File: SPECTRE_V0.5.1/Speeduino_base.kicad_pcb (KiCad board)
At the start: 2 copper layers, 100 x 93 mm, 205 parts, among them J1 Conn_01x06_Male, J2 Conn_02x04_Odd_Even, Q1 AO3400, Q12 BSP78, Q13 BSP78, Q14 BSP78, Q15 BSP78, Q18 BSP78, Q19 BSP78, Q2 AO3400, Q20 BSP78, Q23 BSP78, Q24 BSP78, Q25 BSP78, Q26 BSP78, Q27 AO3400, Q28 AO3400, Q3 AO3400, Q4 AO3400, Q5 AO3400, Q6 AO3400, Q7 AO3400, U1 MAX9926UAEE+, U2 LM78M05_TO220, U3 TL431DBZ, U4 molex_48pin, U5 TJA1050, U6 MAX3232

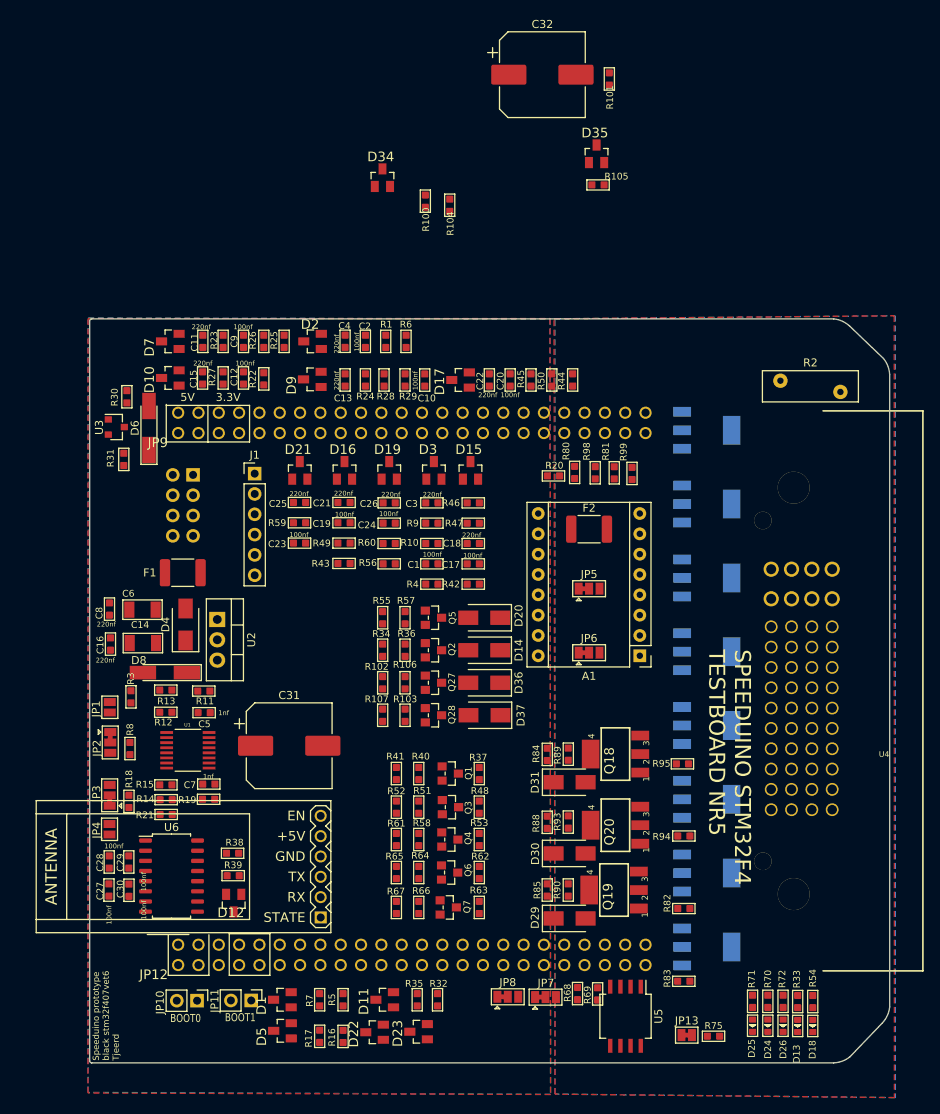
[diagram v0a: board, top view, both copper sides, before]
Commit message: re-add bluetooth module
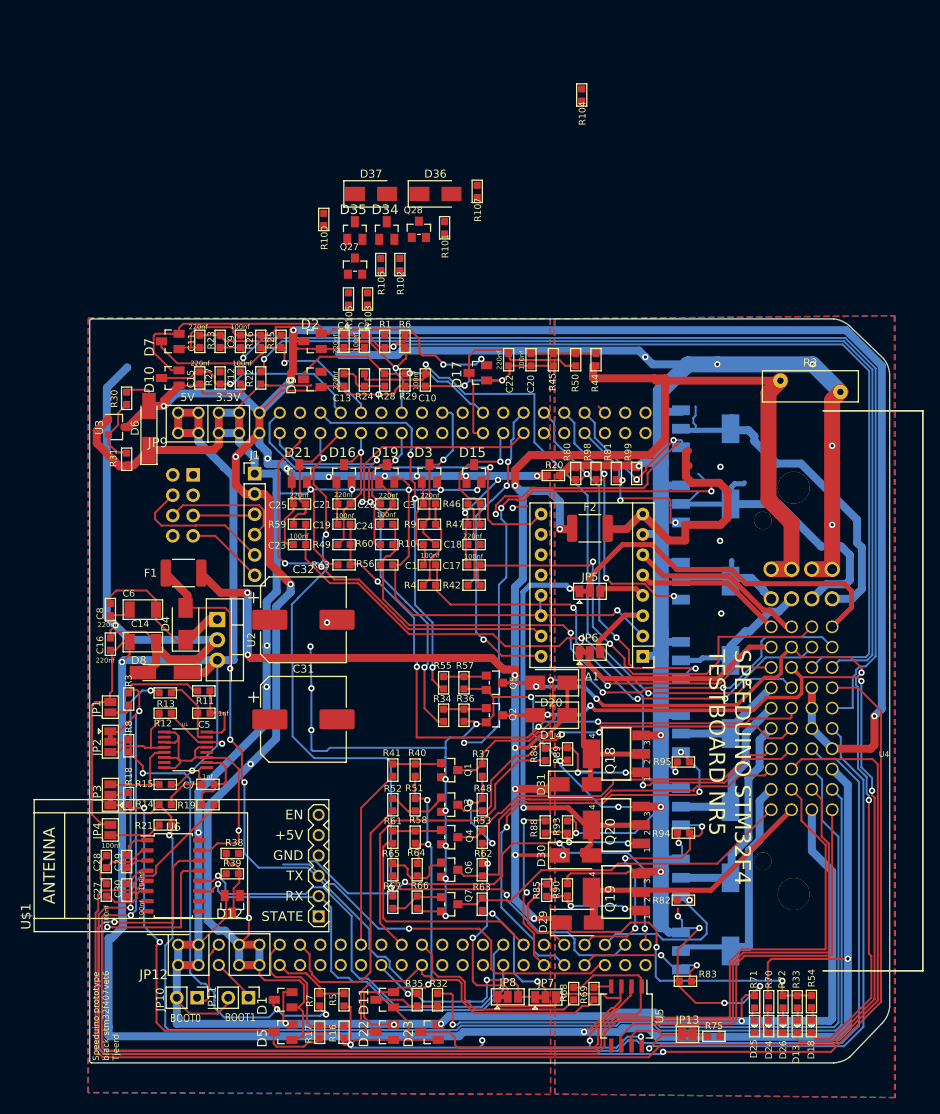
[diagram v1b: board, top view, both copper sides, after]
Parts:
- moved C32 74.4 mm to (140.7, 54.6)
- moved D37 66.7 mm to (149.2, 1.38), turned to 0 degrees
- moved R107 66.5 mm to (162.4, 1.06), turned to 0 degrees
- moved D36 61.4 mm to (157.2, 1.38), turned to 0 degrees
- moved Q28 60.8 mm to (155.2, 5.81), turned to 0 degrees
- moved Q27 53.0 mm to (147.2, 10.4), turned to 0 degrees
- moved R106 52.4 mm to (150.4, 10.2)
- moved R102 52.3 mm to (152.8, 10.2), turned to 0 degrees
- moved R103 52.2 mm to (148.7, 14.5), turned to 0 degrees
- moved R105 34.3 mm to (146.3, 14.5), turned to 0 degrees
- moved D35 31.7 mm to (147.1, 5.95)
- moved R101 27.8 mm to (158.4, 5.61)
- moved R104 21.5 mm to (175.5, -11.0)
- moved R100 12.9 mm to (143.3, 4.57)
- moved D14 11.7 mm to (171.7, 66.5)
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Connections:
- C1 pad 2: AIN_1 -> AIN_2
- C2 pad 2: AIN_0 -> AIN_1
- C24 pad 2: AIN_2 -> AIN_3
- C32 pad 1: Net-(C32-Pad1) -> 5V
- R1 pad 1: AIN_0 -> AIN_1
- R4 pad 1: AIN_1 -> AIN_2
- R56 pad 1: AIN_2 -> AIN_3
- R6 pad 1: AIN_0 -> AIN_1
- R60 pad 1: AIN_2 -> AIN_3
- U4 pad 14: AIN_1 -> AIN_2
- U4 pad 18: AIN_0 -> AIN_1
- U4 pad 20: AIN_2 -> AIN_3
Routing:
- net GND: track 0.00 -> 597.8 mm, vias 0 -> 25
- net 3.3V: track 0.00 -> 467.7 mm, vias 0 -> 18
- net PWR_GND: track 0.00 -> 456.4 mm, vias 0 -> 30
- net 5V: track 0.00 -> 331.9 mm, vias 0 -> 5
- net VBAT: track 0.00 -> 267.2 mm, vias 0 -> 12
- net VR1+: track 0.00 -> 186.2 mm, vias 0 -> 2
- net VR2-: track 0.00 -> 181.9 mm
- net RS232_TX: track 0.00 -> 179.6 mm, vias 0 -> 2
- net VR1-: track 0.00 -> 174.3 mm, vias 0 -> 2
- net RS232_RX: track 0.00 -> 167.9 mm, vias 0 -> 1
- net VR2+: track 0.00 -> 151.8 mm, vias 0 -> 1
- net MAP: track 0.00 -> 132.1 mm, vias 0 -> 1
- net IAT: track 0.00 -> 121.5 mm, vias 0 -> 1
- net AIN_1: track 0.00 -> 111.4 mm, vias 0 -> 1
- net FUEL_PUMP: track 0.00 -> 105.4 mm, vias 0 -> 4
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
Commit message: Clean-up PCB V0.5.1
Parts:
- removed D34, D35: BAT54S, Speeduino_base:SOT23
- removed R100, R101, R104, R105: 1k, Speeduino_base:R0603
- added D27: YEL, Speeduino_base:LED-0603, F.Cu at (165.9, 19.1)
- added JP14: SolderJumper_3_Bridged12, Jumper:SolderJumper-3_P1.3mm_Bridged12_Pad1.0x1.5mm, F.Cu at (194.3, 53.3)
- added JP15: SolderJumper_3_Bridged12, Jumper:SolderJumper-3_P1.3mm_Bridged12_Pad1.0x1.5mm, F.Cu at (190.5, 53.3)
- added Q8: AO3400, Speeduino_base:SOT-23, F.Cu at (158.5, 20.1)
- added R73: 100R, Speeduino_base:R0603, F.Cu at (162.1, 19.1)
- C31, C32: value 1000uF -> 470uF 6.3V; footprint Capacitor_SMD:CP_Elec_10x12.5 -> Capacitor_SMD:CP_Elec_6.3x7.7
- R25: value 4K7 -> 4k7
- R33, R54: value 1k -> 470R
- U2: footprint Package_TO_SOT_THT:TO-220-3_Vertical -> Package_TO_SOT_THT:TO-220-3_Horizontal_TabUp; moved to B.Cu
- moved Q27 55.0 mm to (194.1, 39.1), turned to 270 degrees
- moved D37 49.9 mm to (192.1, 26.9)
- moved R106 49.6 mm to (190.8, 39.1)
- moved D36 48.8 mm to (192.1, 35.6)
- moved Q28 46.1 mm to (194.1, 30.5), turned to 270 degrees
- moved R102 45.7 mm to (188.2, 39.1), turned to 180 degrees
- moved R103 42.6 mm to (188.2, 30.5)
- moved C31 42.5 mm to (117.9, 102.9), turned to 270 degrees
- moved R107 40.8 mm to (190.8, 30.5)
- moved C32 39.7 mm to (117.9, 22.1), turned to 270 degrees
- moved D6 4.57 mm to (121.4, 35.2)
- moved R31 4.57 mm to (118.6, 39.1)
- moved R30 4.57 mm to (118.6, 31.5)
- moved U3 4.57 mm to (117.3, 35.1)
- moved JP8 0.91 mm to (165.4, 101.7)
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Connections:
- JP9 pad 29: Net-(JP9-Pad29) -> PA6
- R102 pad 1: PD11 -> PB12
- R103 pad 1: PE4 -> PB13
- U4 pad 11: STEP_2B_OUT -> Net-(JP14-Pad2)
- U4 pad 12: STEP_1B_OUT -> Net-(JP15-Pad2)
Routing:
- net GND: track 597.8 -> 665.9 mm, vias 25 -> 120
- net Net-(Q11-Pad1): track 63.2 -> 0.00 mm, vias 3 -> 0
- net PD8: track 58.6 -> 0.00 mm, vias 3 -> 0
- net PD11: track 48.4 -> 0.73 mm, vias 1 -> 0
- net 5V: track 331.9 -> 373.9 mm
- net Spare_2-Out: track 0.00 -> 39.0 mm, vias 0 -> 4
- net 3.3V: track 467.7 -> 504.5 mm, vias 18 -> 17
- net VBAT: track 267.2 -> 302.0 mm, vias 12 -> 10
- net Net-(Q22-Pad1): track 28.2 -> 0.00 mm, vias 1 -> 0
- net PWR_GND: track 456.4 -> 483.8 mm, vias 30 -> 94
- net V_IDLE: track 32.6 -> 5.19 mm
- net Spare_1-Out: track 0.00 -> 25.3 mm, vias 0 -> 2
- net PA9: track 54.7 -> 72.3 mm
- net PA6: track 0.00 -> 15.0 mm
- net PB12: track 0.00 -> 13.9 mm, vias 0 -> 1
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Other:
- board text added: "Black STM32f407vet6"
- board text added: "SPECTRE STM32F4 Speeduino compatible V0.5.1"
- board text removed: "SPEEDUINO STM32F4 TESTBOARD NR5"
- board text removed: "Speeduino prototype black stm32f407vet6 Tjeerd"

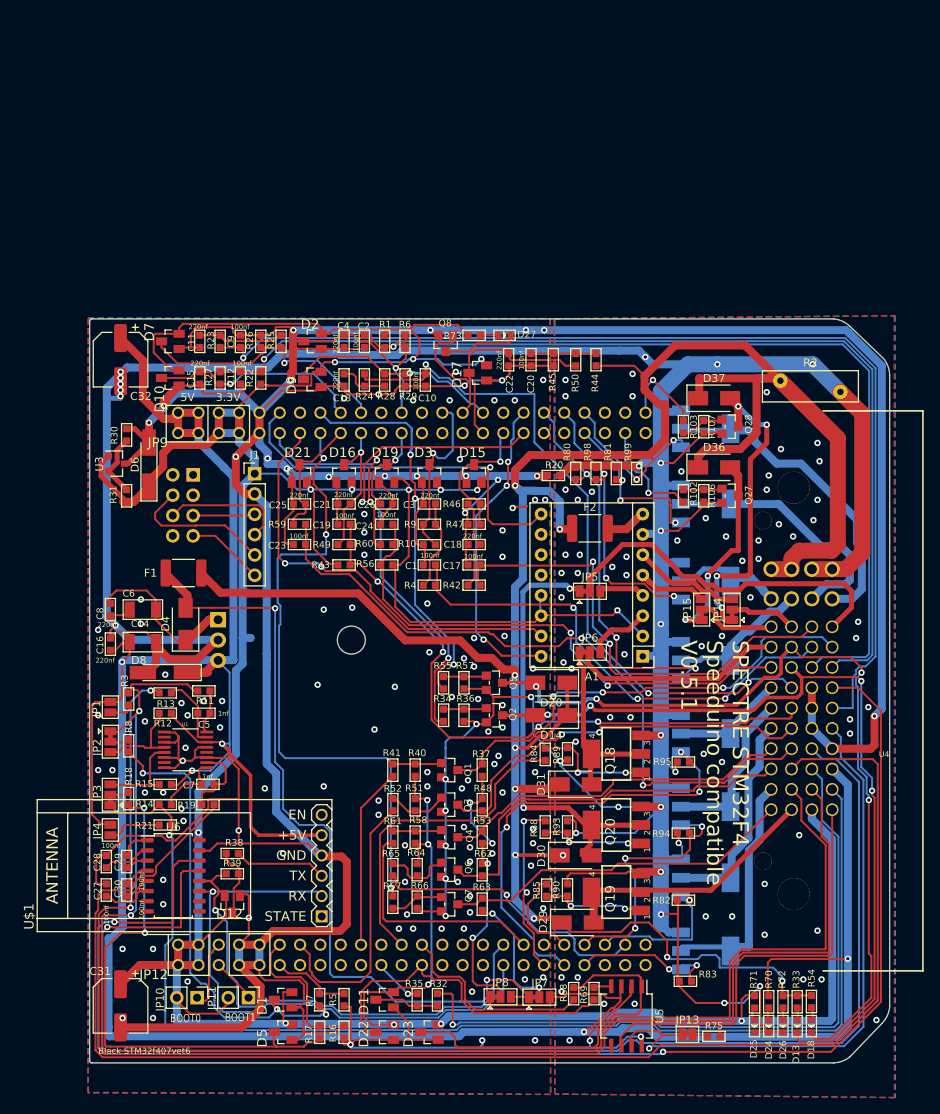
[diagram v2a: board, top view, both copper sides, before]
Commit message: Renumbered all parts from start
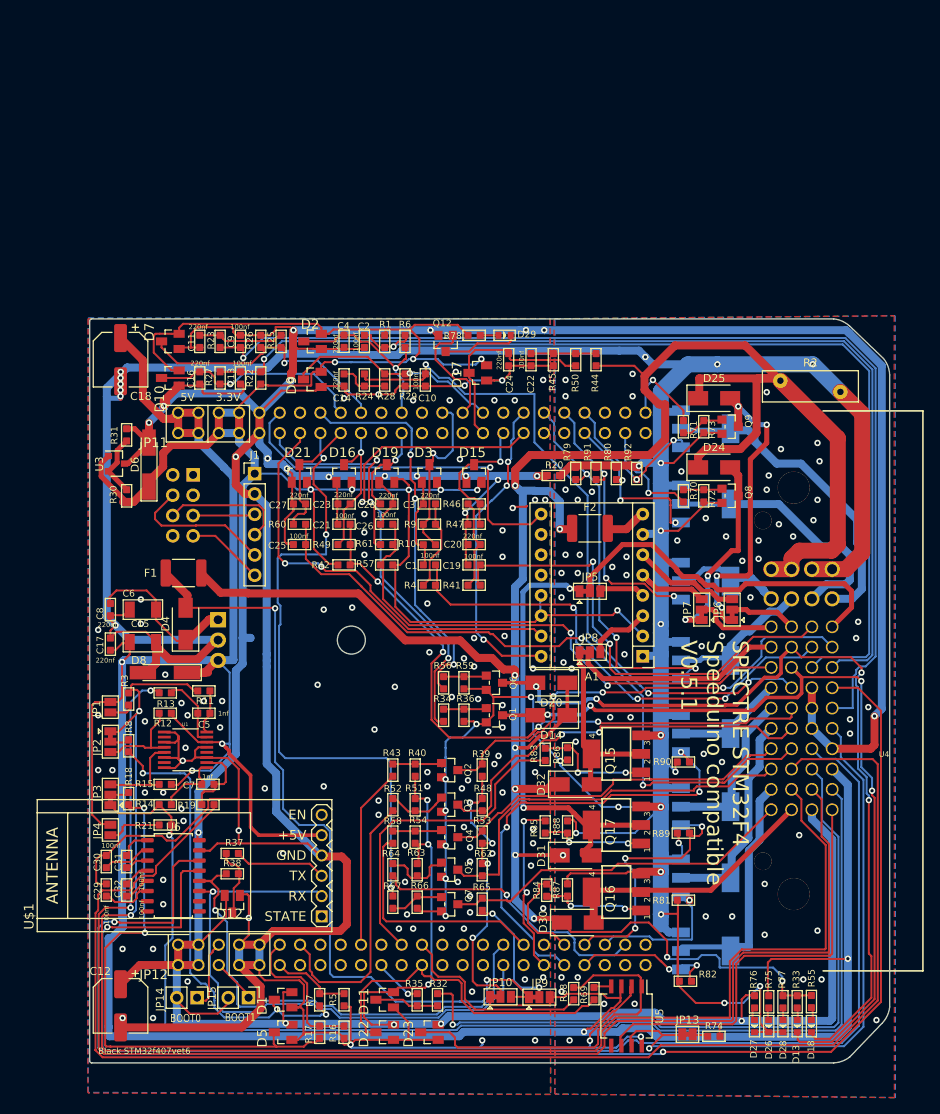
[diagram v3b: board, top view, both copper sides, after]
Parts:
- renumbered C31 to C12, C12 to C13, C13 to C14, C14 to C15, C15 to C16, C16 to C17, C32 to C18, C17 to C19, C18 to C20, C19 to C21, C20 to C22, C21 to C23, C22 to C24, C23 to C25, C24 to C26, C25 to C27, C26 to C28, C27 to C29, C28 to C30, C29 to C31, C30 to C32, D36 to D24, D37 to D25, D24 to D26, D25 to D27, D26 to D28, D27 to D29, D29 to D30, D30 to D31, D31 to D32, JP8 to JP10, JP9 to JP11, JP10 to JP14, JP11 to JP15, JP14 to JP6, JP15 to JP7, JP6 to JP8, JP7 to JP9, Q2 to Q1, Q12 to Q10, Q13 to Q11, Q8 to Q12, Q14 to Q13, Q15 to Q14, Q18 to Q15, Q19 to Q16, Q20 to Q17, Q23 to Q18, Q24 to Q19, Q1 to Q2, Q25 to Q20, Q26 to Q21, Q6 to Q5, Q5 to Q6, Q27 to Q8, Q28 to Q9, R31 to R30, R30 to R31, R38 to R37, R39 to R38, R37 to R39, R42 to R41, R43 to R42, R41 to R43, R58 to R54, R54 to R55, R55 to R56, R56 to R57, R61 to R58, R57 to R59, R59 to R60, R60 to R61, R64 to R63, R65 to R64, R63 to R65, R102 to R70, R103 to R71, R106 to R72, R107 to R73, R75 to R74, R70 to R75, R71 to R76, R72 to R77, R73 to R78, R80 to R79, R81 to R80, R82 to R81, R83 to R82, R84 to R83, R85 to R84, R88 to R85, R89 to R86, R90 to R87, R93 to R88, R94 to R89, R95 to R90, R98 to R91, R99 to R92

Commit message: update molex 48 pin to correct location
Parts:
- U4: footprint rusefi_lib:Molex_48 -> Speeduino_base:Molex_48
